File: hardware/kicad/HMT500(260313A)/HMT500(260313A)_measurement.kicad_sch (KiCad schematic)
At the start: 14 parts, among them J3 SM04B-SRSS-TB, U5 PCAP04-AQFM-24, U6 ADS1220IPWR

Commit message: Footprints and part numbers: no TBD left in the schematic
- Project footprint library hardware/kicad/lib/HMT500_260313A.pretty:
  KiCad 7.0.11 footprints + gen_footprints.py (LMR36006 RNX0012A from TI
  land pattern, Bourns 2035-xx-SM GDT, TVS3301 DRB with floating pad)
- GDT changed to 2-electrode Bourns 2035-23-SM-RPLF (2038 is 3-electrode)
- L1 Wurth WE-SL2 744222 (1 mH, 0.8 A); CMC pins renumbered to WE-SL2
  windings 1-4 / 2-3
- J5 Harwin S1941-46R, L2 Coilcraft XGL4030-153MEC, TPS26611 SOT-23-8,
  TPS2660 HTSSOP-16 footprint from 7.0.11
- R1 MMB02070C4708FB200, R30/R40 CRCW251210R0FKEGHP confirmed;
  R19 -> Vishay PLTT0603 0.02 % 5 ppm
- fp-lib-table written by the generator; netlist 74/74, tests pass

Co-Authored-By: Claude Opus 5.5 <noreply@anthropic.com>
Claude-Session: https://claude.ai/code/session_01JA2o8uJsqp9Vzsg4b665ev
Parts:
- R19: value 4.02k 0.01% 5ppm -> 4.02k 0.02% 5ppm
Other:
- note added: "4.02k 0.02% 5ppm"
- note removed: "4.02k 0.01% 5ppm"
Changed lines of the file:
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@@
 (symbol (lib_id "HMT500_260313A:R") (at 92.71 170.18 90) (unit 1) (in_bom yes) (on_board yes) (dnp no) (property "Reference" "R18" (at 92.71 165.354 90) (effects (font (size 1.27 1.27) bold))) (property "Value" "1k" (at 92.71 167.64 90) (effects (font (size 1.27 1.27)))) (property "Footprint" "Resistor_SMD:R_0603_1608Metric" (at 92.71 170.18 0) (effects (font (size 1.27 1.27)) hide)) (property "Datasheet" "~" (at 92.71 170.18 0) (effects (font (size 1.27 1.27)) hide)) (pin "1") (pin "2") (instances (project "HMT500(260313A)" (path "/1ebb025b-11bd-5f7c-aaab-41e2a750e8b3/c2b6f59b-84fc-5243-aa02-a63f04edae17" (reference "R18") (unit 1)))))
 (symbol (lib_id "HMT500_260313A:C") (at 101.6 166.37 0) (unit 1) (in_bom yes) (on_board yes) (dnp no) (property "Reference" "C27" (at 105.029 157.607 0) (effects (font (size 1.27 1.27) bold) (justify left))) (property "Value" "10n" (at 105.029 159.893 0) (effects (font (size 1.27 1.27)) (justify left))) (property "Footprint" "Capacitor_SMD:C_0603_1608Metric" (at 101.6 166.37 0) (effects (font (size 1.27 1.27)) hide)) (property "Datasheet" "~" (at 101.6 166.37 0) (effects (font (size 1.27 1.27)) hide)) (pin "1") (pin "2") (instances (project "HMT500(260313A)" (path "/1ebb025b-11bd-5f7c-aaab-41e2a750e8b3/c2b6f59b-84fc-5243-aa02-a63f04edae17" (reference "C27") (unit 1)))))
-(symbol (lib_id "HMT500_260313A:R") (at 130.81 184.15 0) (unit 1) (in_bom yes) (on_board yes) (dnp no) (property "Reference" "R19" (at 128.397 183.007 0) (effects (font (size 1.27 1.27) bold) (justify right))) (property "Value" "4.02k 0.01% 5ppm" (at 128.397 185.293 0) (effects (font (size 1.27 1.27)) (justify right))) (property "Footprint" "Resistor_SMD:R_0603_1608Metric" (at 130.81 184.15 0) (effects (font (size 1.27 1.27)) hide)) (property "Datasheet" "~" (at 130.81 184.15 0) (effects (font (size 1.27 1.27)) hide)) (pin "1") (pin "2") (instances (project "HMT500(260313A)" (path "/1ebb025b-11bd-5f7c-aaab-41e2a750e8b3/c2b6f59b-84fc-5243-aa02-a63f04edae17" (reference "R19") (unit 1)))))
+(symbol (lib_id "HMT500_260313A:R") (at 130.81 184.15 0) (unit 1) (in_bom yes) (on_board yes) (dnp no) (property "Reference" "R19" (at 128.397 183.007 0) (effects (font (size 1.27 1.27) bold) (justify right))) (property "Value" "4.02k 0.02% 5ppm" (at 128.397 185.293 0) (effects (font (size 1.27 1.27)) (justify right))) (property "Footprint" "Resistor_SMD:R_0603_1608Metric" (at 130.81 184.15 0) (effects (font (size 1.27 1.27)) hide)) (property "Datasheet" "~" (at 130.81 184.15 0) (effects (font (size 1.27 1.27)) hide)) (pin "1") (pin "2") (instances (project "HMT500(260313A)" (path "/1ebb025b-11bd-5f7c-aaab-41e2a750e8b3/c2b6f59b-84fc-5243-aa02-a63f04edae17" (reference "R19") (unit 1)))))
 (symbol (lib_id "HMT500_260313A:R") (at 138.43 191.77 0) (unit 1) (in_bom yes) (on_board yes) (dnp no) (property "Reference" "R20" (at 140.843 190.627 0) (effects (font (size 1.27 1.27) bold) (justify left))) (property "Value" "1k" (at 140.843 192.913 0) (effects (font (size 1.27 1.27)) (justify left))) (property "Footprint" "Resistor_SMD:R_0603_1608Metric" (at 138.43 191.77 0) (effects (font (size 1.27 1.27)) hide)) (property "Datasheet" "~" (at 138.43 191.77 0) (effects (font (size 1.27 1.27)) hide)) (pin "1") (pin "2") (instances (project "HMT500(260313A)" (path "/1ebb025b-11bd-5f7c-aaab-41e2a750e8b3/c2b6f59b-84fc-5243-aa02-a63f04edae17" (reference "R20") (unit 1)))))
 (symbol (lib_id "HMT500_260313A:GND") (at 138.43 198.12 0) (unit 1) (in_bom no) (on_board no) (dnp no) (property "Reference" "#PWR067" (at 138.43 204.47 0) (effects (font (size 1.27 1.27) bold) hide)) (property "Value" "GND" (at 138.43 205.74 0) (effects (font (size 1.27 1.27) italic) hide)) (property "Footprint" "" (at 138.43 198.12 0) (effects (font (size 1.27 1.27)) hide)) (property "Datasheet" "~" (at 138.43 198.12 0) (effects (font (size 1.27 1.27)) hide)) (pin "1") (instances (project "HMT500(260313A)" (path "/1ebb025b-11bd-5f7c-aaab-41e2a750e8b3/c2b6f59b-84fc-5243-aa02-a63f04edae17" (reference "#PWR067") (unit 1)))))
@@
 (text "24비트 ADC, 50/60 Hz 제거, 내부 온도센서 (PCB 온도). 설정 한계: IDAC ≤ 250 uA, PGA ≤ 2 (SPI1 모드 1)" (at 140.198 253.746 0) (effects (font (face "NanumGothic") (size 1.27 1.27)) (justify left bottom)))
 (text "R19" (at 67.31 258.064 0) (effects (font (size 1.27 1.27) bold) (justify left bottom)))
-(text "4.02k 0.01% 5ppm" (at 89.5883 258.064 0) (effects (font (size 1.27 1.27)) (justify left bottom)))
+(text "4.02k 0.02% 5ppm" (at 89.5883 258.064 0) (effects (font (size 1.27 1.27)) (justify left bottom)))
 (text "Pt1000 비율 측정 기준저항" (at 114.48 258.064 0) (effects (font (face "NanumGothic") (size 1.27 1.27)) (justify left bottom)))
 (text "IDAC 전류 오차 상쇄, 온도계수 5 ppm/°C" (at 140.198 258.064 0) (effects (font (face "NanumGothic") (size 1.27 1.27)) (justify left bottom)))

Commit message: Schematic v0.9 + placement rev 4: apply triple-review A/B items, re-review fixes
- Power: OVP 32.6 V (R5 36.5k), D2 TVS3301, C2 2.2u 100V, buck input 220n x2,
  U2 pin 3 = SW; TPS26611 +Vs emitter-follower clamp (Q1 MMBTA06, R50, D50 27V)
- RS-485: THVD2410, DE 10k pull-down (R60) for in-house bootloader
- MCU: SGOOD on PA0/PA4, CS_CDC PA15, VIN_SENSE PB0, LATCH/CS pull-ups,
  SWD no-connect removed, netlist checker flags no-connect on used pins
- Analog: OPA197 V+ = DAC AVDD, R31/R41 100k, local caps; X7R throughout
- New aux sheet; SOT-23 and R1206 footprints; parts list and JLC files
- Placement: pin-targeted hints, MCU decaps under U4, chassis parts grouped
  in front, J5 keep-out 3.3 mm, CHASSIS netclass; 102/102 parts placed
- Docs: final review H table, decision #32, circuit design, placement rev 4

Co-Authored-By: Claude Opus 5.5 <noreply@anthropic.com>
Claude-Session: https://claude.ai/code/session_01JA2o8uJsqp9Vzsg4b665ev
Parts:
- C24: value 10u -> 22u 10V; footprint Capacitor_SMD:C_0805_2012Metric -> Capacitor_SMD:C_1206_3216Metric
- C25: value 4.7u -> 10u; footprint Capacitor_SMD:C_0805_2012Metric -> Capacitor_SMD:C_1206_3216Metric
- C27: value 10n -> 10n C0G
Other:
- note added: "10u / 22u"
- note added: "1k / 10n C0G"
- note added: "MK33-W mini (200 pF)와 비슷한 값, C0G. MK33-W (300 pF)면 270–330 pF (센서 품번 확정 후)"
- note added: "VDD18 ≥ 4.7 uF, VDD33 ≥ 10 uF (데이터시트 표 2) — DC 바이어스 후에도 충족 (v0.9)"
- note added: "차동 노이즈 제거 (C0G, 데이터시트 9.2)"
- note removed: "1k / 10n"
- note removed: "4.7u / 10u"
- note removed: "MK33-W mini (200 pF)와 비슷한 값, C0G (온도 변화 거의 없음)"
- note removed: "VDD18 ≥ 4.7 uF, VDD33 ≥ 10 uF (데이터시트 표 2)"
- note removed: "차동·공통모드 노이즈 제거"

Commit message: Decision #33: keep TPS26611, JST connectors, MK33-W 300 pF (C22 330 pF), JLC parts
Co-Authored-By: Claude Opus 5.5 <noreply@anthropic.com>
Claude-Session: https://claude.ai/code/session_01JA2o8uJsqp9Vzsg4b665ev
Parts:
- C22: value 220p C0G 1% -> 330p C0G 1%
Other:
- note added: "330p C0G 1%"
- note added: "센서 MK33-W (300 pF, 결정 #33) 측정 범위 가운데 값, C0G"
- note removed: "220p C0G 1%"
- note removed: "MK33-W mini (200 pF)와 비슷한 값, C0G. MK33-W (300 pF)면 270–330 pF (센서 품번 확정 후)"
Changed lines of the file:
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@@
 (symbol (lib_id "HMT500_260313A:CONN_SH4") (at 30.48 137.16 0) (unit 1) (in_bom yes) (on_board yes) (dnp no) (property "Reference" "J3" (at 22.86 128.27 0) (effects (font (size 1.27 1.27) bold) (justify left))) (property "Value" "SM04B-SRSS-TB" (at 22.86 130.556 0) (effects (font (size 1.27 1.27)) (justify left))) (property "Footprint" "Connector_JST:JST_SH_SM04B-SRSS-TB_1x04-1MP_P1.00mm_Horizontal" (at 30.48 137.16 0) (effects (font (size 1.27 1.27)) hide)) (property "Datasheet" "~" (at 30.48 137.16 0) (effects (font (size 1.27 1.27)) hide)) (pin "1") (pin "2") (pin "3") (pin "4") (instances (project "HMT500(260313A)" (path "/1ebb025b-11bd-5f7c-aaab-41e2a750e8b3/c2b6f59b-84fc-5243-aa02-a63f04edae17" (reference "J3") (unit 1)))))
 (symbol (lib_id "HMT500_260313A:PCAP04") (at 142.24 73.66 0) (unit 1) (in_bom yes) (on_board yes) (dnp no) (property "Reference" "U5" (at 156.464 54.61 0) (effects (font (size 1.27 1.27) bold) (justify left))) (property "Value" "PCAP04-AQFM-24" (at 156.464 56.896 0) (effects (font (size 1.27 1.27)) (justify left))) (property "Footprint" "Package_DFN_QFN:QFN-24-1EP_4x4mm_P0.5mm_EP2.6x2.6mm" (at 142.24 73.66 0) (effects (font (size 1.27 1.27)) hide)) (property "Datasheet" "~" (at 142.24 73.66 0) (effects (font (size 1.27 1.27)) hide)) (pin "24") (pin "1") (pin "22") (pin "20") (pin "21") (pin "23") (pin "19") (pin "6") (pin "5") (pin "7") (pin "9") (pin "16") (pin "15") (pin "10") (pin "11") (pin "12") (pin "17") (pin "18") (pin "3") (pin "13") (pin "4") (pin "14") (pin "2") (pin "8") (pin "25") (instances (project "HMT500(260313A)" (path "/1ebb025b-11bd-5f7c-aaab-41e2a750e8b3/c2b6f59b-84fc-5243-aa02-a63f04edae17" (reference "U5") (unit 1)))))
-(symbol (lib_id "HMT500_260313A:C") (at 119.38 69.85 0) (unit 1) (in_bom yes) (on_board yes) (dnp no) (property "Reference" "C22" (at 115.951 68.707 0) (effects (font (size 1.27 1.27) bold) (justify right))) (property "Value" "220p C0G 1%" (at 115.951 70.993 0) (effects (font (size 1.27 1.27)) (justify right))) (property "Footprint" "Capacitor_SMD:C_0603_1608Metric" (at 119.38 69.85 0) (effects (font (size 1.27 1.27)) hide)) (property "Datasheet" "~" (at 119.38 69.85 0) (effects (font (size 1.27 1.27)) hide)) (pin "1") (pin "2") (instances (project "HMT500(260313A)" (path "/1ebb025b-11bd-5f7c-aaab-41e2a750e8b3/c2b6f59b-84fc-5243-aa02-a63f04edae17" (reference "C22") (unit 1)))))
+(symbol (lib_id "HMT500_260313A:C") (at 119.38 69.85 0) (unit 1) (in_bom yes) (on_board yes) (dnp no) (property "Reference" "C22" (at 115.951 68.707 0) (effects (font (size 1.27 1.27) bold) (justify right))) (property "Value" "330p C0G 1%" (at 115.951 70.993 0) (effects (font (size 1.27 1.27)) (justify right))) (property "Footprint" "Capacitor_SMD:C_0603_1608Metric" (at 119.38 69.85 0) (effects (font (size 1.27 1.27)) hide)) (property "Datasheet" "~" (at 119.38 69.85 0) (effects (font (size 1.27 1.27)) hide)) (pin "1") (pin "2") (instances (project "HMT500(260313A)" (path "/1ebb025b-11bd-5f7c-aaab-41e2a750e8b3/c2b6f59b-84fc-5243-aa02-a63f04edae17" (reference "C22") (unit 1)))))
 (symbol (lib_id "HMT500_260313A:+3V3A") (at 138.43 53.34 0) (unit 1) (in_bom no) (on_board no) (dnp no) (property "Reference" "#PWR071" (at 138.43 45.212 0) (effects (font (size 1.27 1.27) bold) hide)) (property "Value" "+3V3A" (at 138.43 47.498 0) (effects (font (size 1.27 1.27) italic))) (property "Footprint" "" (at 138.43 53.34 0) (effects (font (size 1.27 1.27)) hide)) (property "Datasheet" "~" (at 138.43 53.34 0) (effects (font (size 1.27 1.27)) hide)) (pin "1") (instances (project "HMT500(260313A)" (path "/1ebb025b-11bd-5f7c-aaab-41e2a750e8b3/c2b6f59b-84fc-5243-aa02-a63f04edae17" (reference "#PWR071") (unit 1)))))
 (symbol (lib_id "HMT500_260313A:+3V3A") (at 146.05 53.34 0) (unit 1) (in_bom no) (on_board no) (dnp no) (property "Reference" "#PWR072" (at 146.05 45.212 0) (effects (font (size 1.27 1.27) bold) hide)) (property "Value" "+3V3A" (at 146.05 47.498 0) (effects (font (size 1.27 1.27) italic))) (property "Footprint" "" (at 146.05 53.34 0) (effects (font (size 1.27 1.27)) hide)) (property "Datasheet" "~" (at 146.05 53.34 0) (effects (font (size 1.27 1.27)) hide)) (pin "1") (instances (project "HMT500(260313A)" (path "/1ebb025b-11bd-5f7c-aaab-41e2a750e8b3/c2b6f59b-84fc-5243-aa02-a63f04edae17" (reference "#PWR072") (unit 1)))))
@@
 (text "VDD18 ≥ 4.7 uF, VDD33 ≥ 10 uF (데이터시트 표 2) — DC 바이어스 후에도 충족 (v0.9)" (at 140.198 245.11 0) (effects (font (face "NanumGothic") (size 1.27 1.27)) (justify left bottom)))
 (text "C22" (at 67.31 249.428 0) (effects (font (size 1.27 1.27) bold) (justify left bottom)))
-(text "220p C0G 1%" (at 89.5883 249.428 0) (effects (font (size 1.27 1.27)) (justify left bottom)))
+(text "330p C0G 1%" (at 89.5883 249.428 0) (effects (font (size 1.27 1.27)) (justify left bottom)))
 (text "PCAP04 기준 용량" (at 114.48 249.428 0) (effects (font (face "NanumGothic") (size 1.27 1.27)) (justify left bottom)))
-(text "MK33-W mini (200 pF)와 비슷한 값, C0G. MK33-W (300 pF)면 270–330 pF (센서 품번 확정 후)" (at 140.198 249.428 0) (effects (font (face "NanumGothic") (size 1.27 1.27)) (justify left bottom)))
+(text "센서 MK33-W (300 pF, 결정 #33) 측정 범위 가운데 값, C0G" (at 140.198 249.428 0) (effects (font (face "NanumGothic") (size 1.27 1.27)) (justify left bottom)))
 (text "U6" (at 67.31 253.746 0) (effects (font (size 1.27 1.27) bold) (justify left bottom)))
 (text "ADS1220IPWR" (at 89.5883 253.746 0) (effects (font (size 1.27 1.27)) (justify left bottom)))

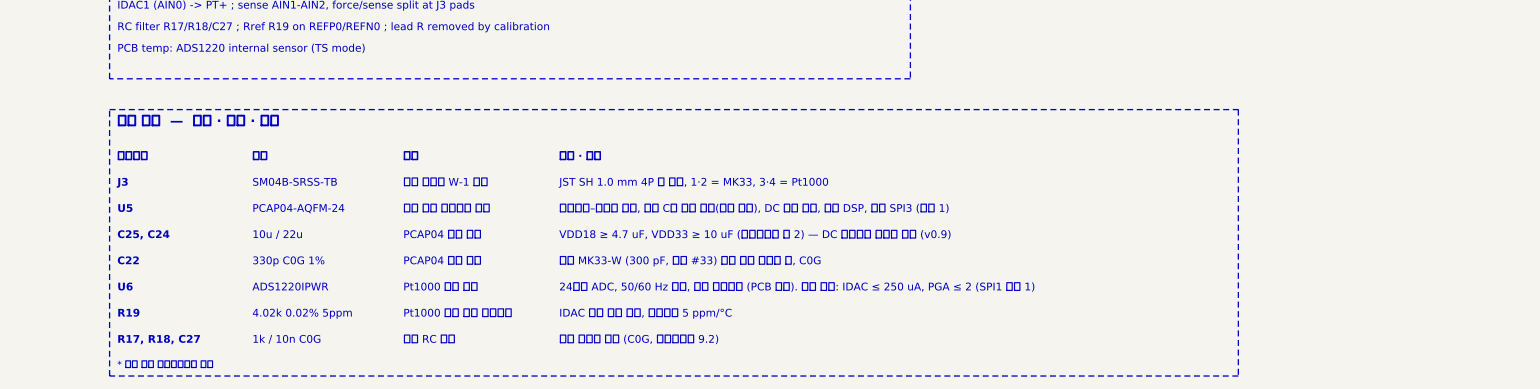
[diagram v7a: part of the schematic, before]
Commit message: Apply agreed external review items (decision #35)
- H01: series 100 V Schottky D3 (PMEG10010ELR) between D2 and eFuse IN
  (new net VIN_D) so negative surges no longer stress U1 IN-OUT
- H02: RS-485 bus TVS D60/D61 (TVS3301); U11 -> THVD2410DGKR (VSSOP-8)
- H04: +Vs clamp zener 27 V -> 24 V (BZX84C24LT1G)
- H08: ADS1220 IDAC fixed at 250 uA
- Room for new parts: C7 removed, 37 low-voltage R/C moved to 0402
  (LCSC basic where available); chassis parts keep CH_GAP between each other
- Placement 104/104, netlist 78/78, pcbnew DRC: no clearance errors,
  assembly sim 23 OK; parts list / JLC BOM updated
- docs/hw/external-review-response-260930.md: item responses, output load
  table, current budget, firmware requirements F1-F6, tests T1-T7

Co-Authored-By: Claude Opus 5.5 <noreply@anthropic.com>
Claude-Session: https://claude.ai/code/session_01JA2o8uJsqp9Vzsg4b665ev
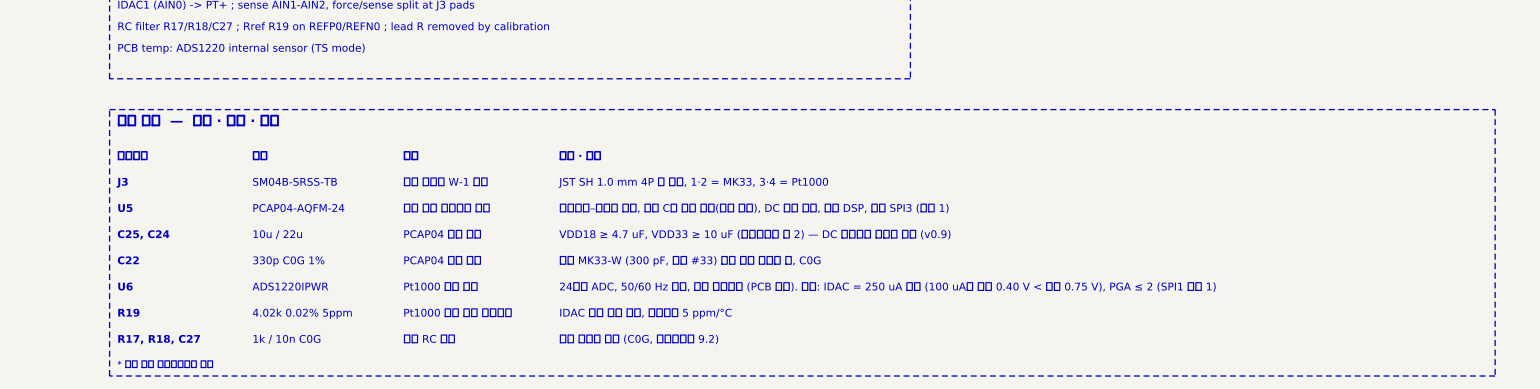
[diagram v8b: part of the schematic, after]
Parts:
- C23, C28, C29: footprint Capacitor_SMD:C_0603_1608Metric -> Capacitor_SMD:C_0402_1005Metric
- R17, R18, R20: footprint Resistor_SMD:R_0603_1608Metric -> Resistor_SMD:R_0402_1005Metric
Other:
- note added: "24비트 ADC, 50/60 Hz 제거, 내부 온도센서 (PCB 온도). 설정: IDAC = 250 uA 고정 (100 uA면 기준 0.40 V < 권장 0.75 V), PGA ≤ 2 (SPI1 모드 1)"
- note removed: "24비트 ADC, 50/60 Hz 제거, 내부 온도센서 (PCB 온도). 설정 한계: IDAC ≤ 250 uA, PGA ≤ 2 (SPI1 모드 1)"
